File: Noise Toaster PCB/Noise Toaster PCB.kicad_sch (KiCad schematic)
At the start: 0 parts

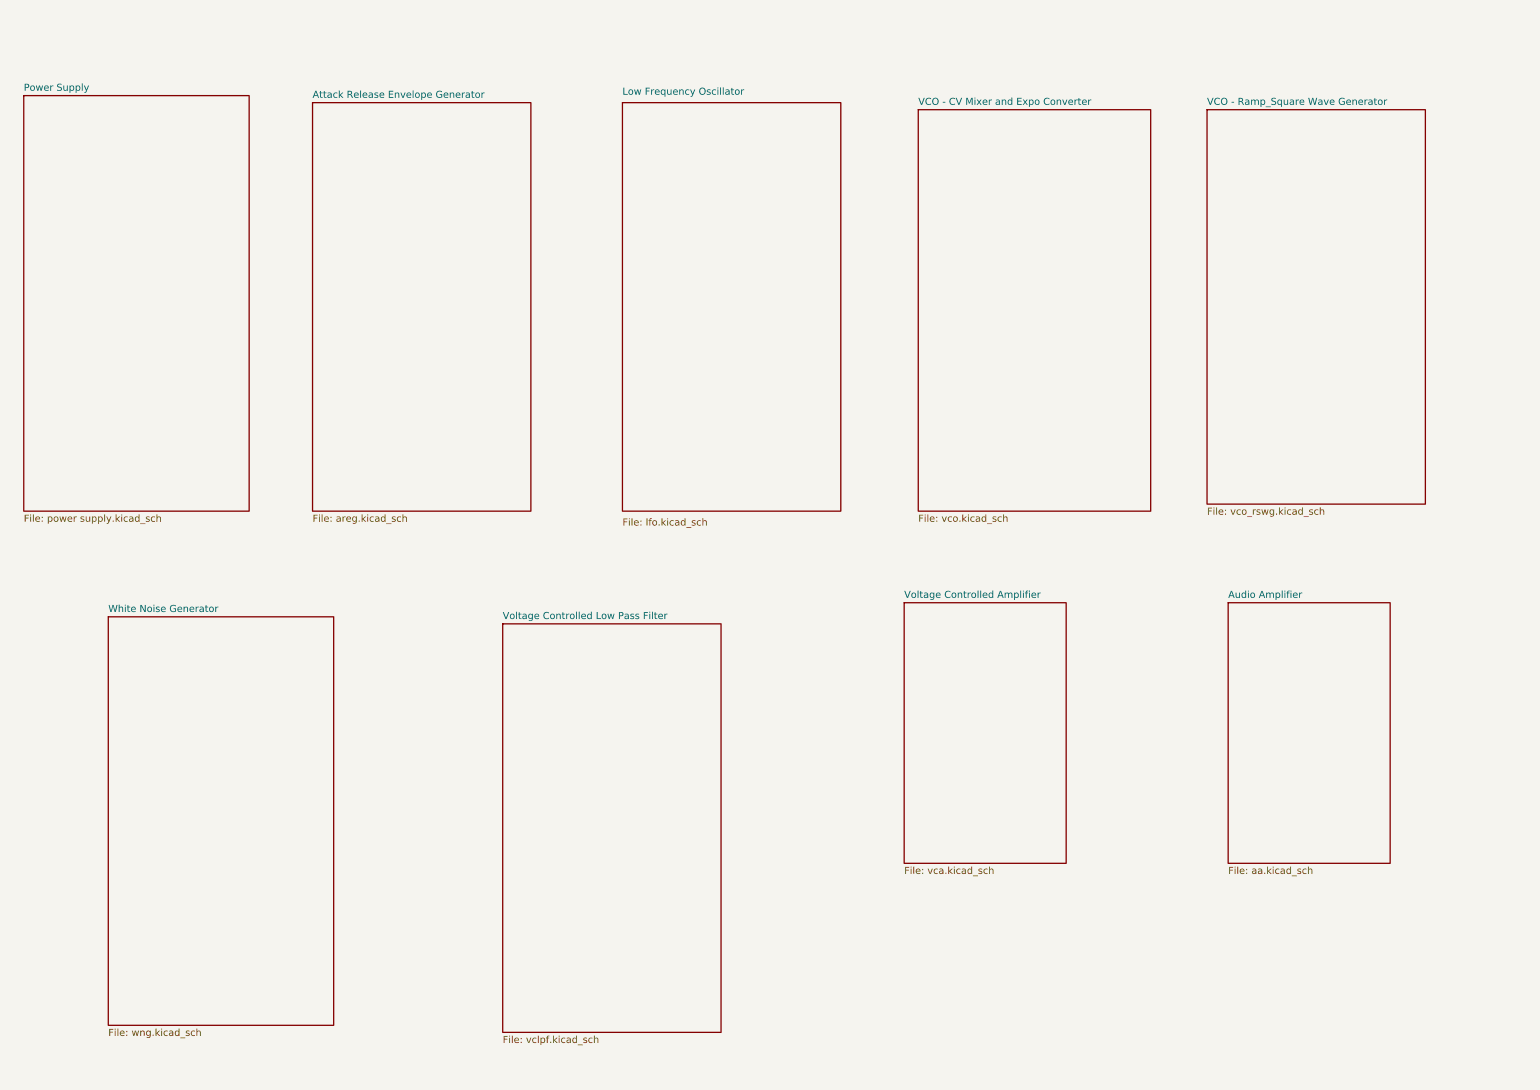
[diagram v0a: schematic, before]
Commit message: updated schematics
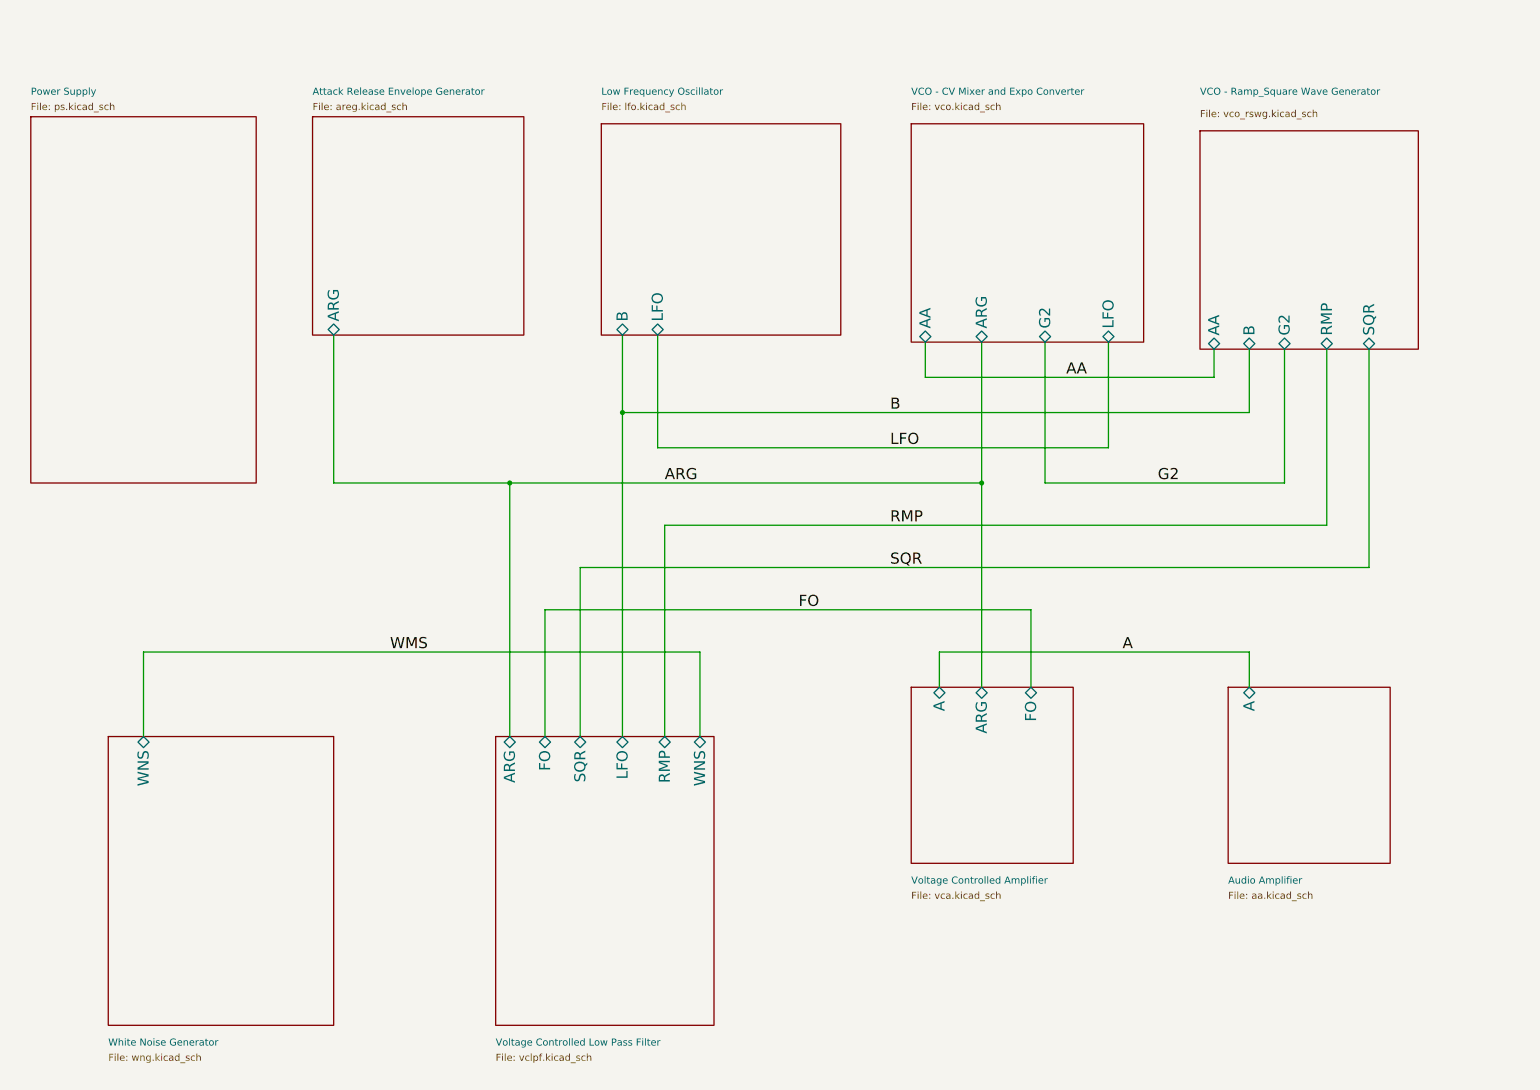
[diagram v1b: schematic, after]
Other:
- sheet Attack Release Envelope Generator ports: added ARG; removed none
- sheet Audio Amplifier ports: added A; removed none
- sheet Low Frequency Oscillator ports: added B, LFO; removed none
- sheet Power Supply: file power supply.kicad_sch -> ps.kicad_sch
- sheet VCO - CV Mixer and Expo Converter ports: added AA, ARG, G2, LFO; removed none
- sheet VCO - Ramp_Square Wave Generator ports: added AA, B, G2, RMP, SQR; removed none
- sheet Voltage Controlled Amplifier ports: added A, ARG, FO; removed none
- sheet Voltage Controlled Low Pass Filter ports: added ARG, FO, LFO, RMP, SQR, WNS; removed none
- sheet White Noise Generator ports: added WNS; removed none

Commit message: refactored the schematic
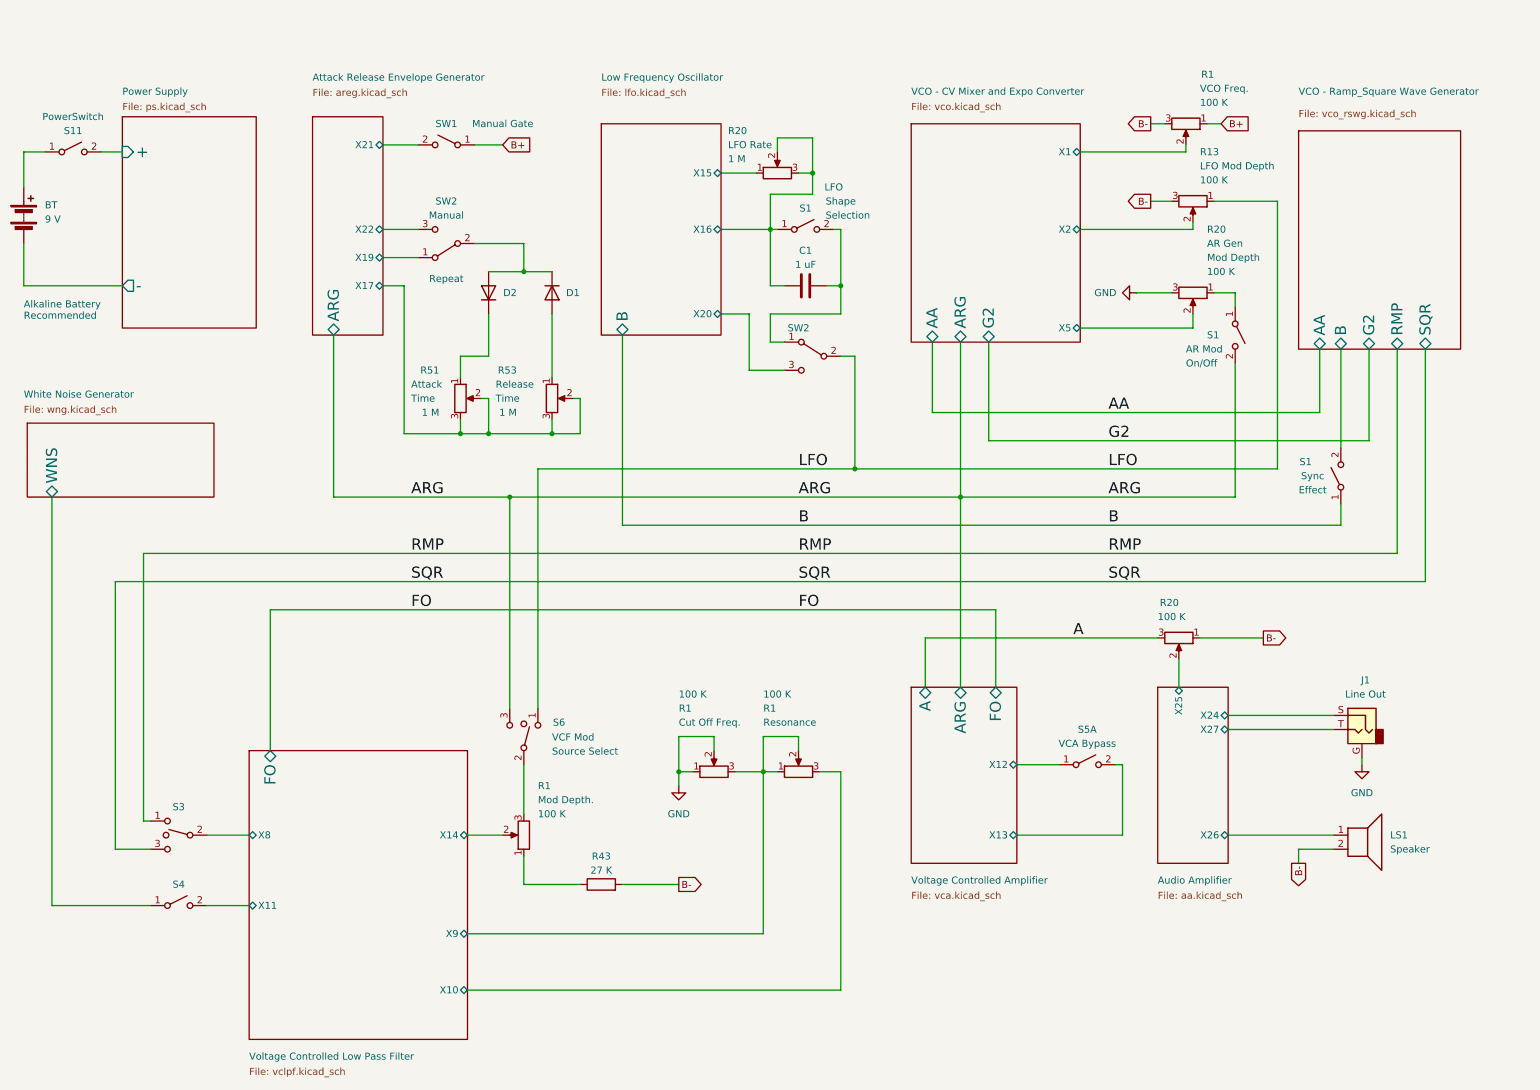
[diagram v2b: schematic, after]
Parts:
- added BT: 9 V, symbol Device:Battery
- added C1: 1 uF, symbol Device:C
- added D1, D2: D, symbol Device:D
- added J1: Line Out, symbol Connector_Audio:AudioJack2_Ground
- added LS1: Speaker, symbol Device:Speaker
- added PowerSwitch: S11, symbol Switch:SW_SPST
- added R1 (x4), R13, R20 (x2): 100 K, symbol Device:R_Potentiometer
- added R20, R51, R53: 1 M, symbol Device:R_Potentiometer
- added R43: 27 K, symbol Device:R
- added S1: LFO, symbol Switch:SW_SPST
- added S1: Sync, symbol Switch:SW_SPST
- added S1: AR Mod, symbol Switch:SW_SPST
- added S3: ~, symbol Switch:SW_SPDT_MSM
- added S4: SW_SPST, symbol Switch:SW_SPST
- added S5: VCA Bypass, symbol Switch:SW_DPST_x2
- added S6: VCF Mod, symbol Switch:SW_SPDT_MSM
- added SW1: Manual Gate, symbol Switch:SW_SPST
- added SW2: ~, symbol Switch:SW_SPDT
- added SW2: Repeat, symbol Switch:SW_SPDT
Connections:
- net A: now also R20.3
- net ARG: now also S1.2 (B), S6.3
- net B: now also S1.1 (A)
- net LFO: now also R13.1, S6.1, SW2.2 (B)
- net RMP: now also S3.1
- net SQR: now also S3.3
- new net: C1.2, S1.2 (B), SW2.1 (A)
- new net: D1.2 (A), R53.1
- new net: D2.1 (K), R51.1
- new net: D1.1 (K), D2.2 (A), SW2.2 (B)
- new net: R1.3, S6.2
- new net: R20.1, S1.1 (A)
- new net: BT.1 (+), PowerSwitch.1 (A)
- new net: R1.1, R43.1
- new net Attack Release Envelope Generator/X17: R51.2, R51.3, R53.2, R53.3
- new net Attack Release Envelope Generator/X19: SW2.1 (A)
- new net Attack Release Envelope Generator/X21: SW1.2 (B)
- new net Attack Release Envelope Generator/X22: SW2.3 (C)
- new net Audio Amplifier/X24: J1.S
- new net Audio Amplifier/X25: R20.2
- new net Audio Amplifier/X26: LS1.1
- new net Audio Amplifier/X27: J1.T
- new net B+: R1.1, SW1.1 (A)
- new net B-: LS1.2, R1.3, R13.3, R20.1, R43.2
- new net GND: J1.G, R1.1, R1.2, R20.3
- new net Low Frequency Oscillator/X15: R20.1
- new net Low Frequency Oscillator/X16: C1.1, R20.2, R20.3, S1.1 (A)
- new net Low Frequency Oscillator/X20: SW2.3 (C)
- new net Power Supply/+: PowerSwitch.2 (B)
- new net Power Supply/-: BT.2 (-)
- new net VCO - CV Mixer and Expo Converter/X1: R1.2
- new net VCO - CV Mixer and Expo Converter/X2: R13.2
- new net VCO - CV Mixer and Expo Converter/X5: R20.2
- new net VCO - Ramp_Square Wave Generator/B: S1.2 (B)
- new net Voltage Controlled Amplifier/X12: S5.1 (A)
- new net Voltage Controlled Amplifier/X13: S5.2 (B)
- new net Voltage Controlled Low Pass Filter/X10: R1.3
- new net Voltage Controlled Low Pass Filter/X11: S4.2 (B)
- new net Voltage Controlled Low Pass Filter/X14: R1.2
- new net Voltage Controlled Low Pass Filter/X8: S3.2
- new net Voltage Controlled Low Pass Filter/X9: R1.1, R1.2, R1.3
- new net White Noise Generator/WNS: S4.1 (A)
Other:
- sheet Attack Release Envelope Generator ports: added X17, X19, X21, X22; removed none
- sheet Audio Amplifier ports: added X24, X25, X26, X27; removed A
- sheet Low Frequency Oscillator ports: added X15, X16, X20; removed LFO
- sheet Power Supply ports: added +, -; removed none
- sheet VCO - CV Mixer and Expo Converter ports: added X1, X2, X5; removed LFO
- sheet Voltage Controlled Amplifier ports: added X12, X13; removed none
- sheet Voltage Controlled Low Pass Filter ports: added X10, X11, X14, X8, X9; removed ARG, LFO, RMP, SQR, WNS
- note added: "Alkaline Battery Recommended"

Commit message: refactored schematics and added front panel
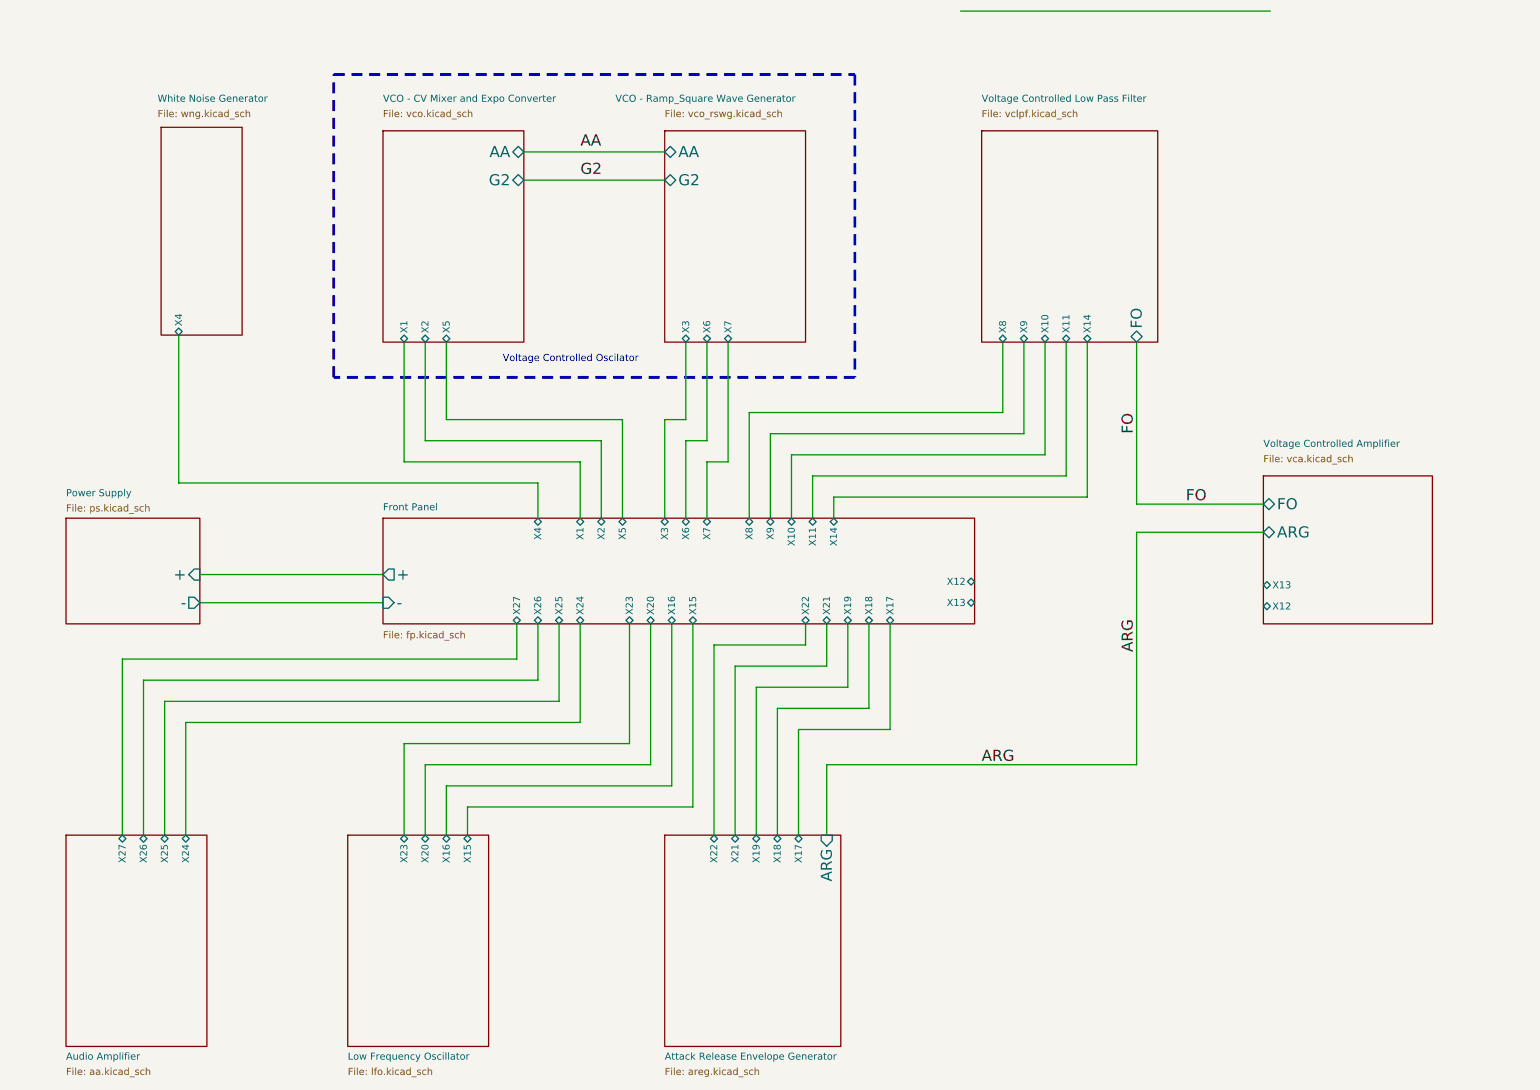
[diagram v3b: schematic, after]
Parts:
- removed BT: 9 V, symbol Device:Battery
- removed C1: 1 uF, symbol Device:C
- removed D1, D2: D, symbol Device:D
- removed J1: Line Out, symbol Connector_Audio:AudioJack2_Ground
- removed LS1: Speaker, symbol Device:Speaker
- removed PowerSwitch: S11, symbol Switch:SW_SPST
- removed R1 (x4), R13, R20 (x2): 100 K, symbol Device:R_Potentiometer
- removed R20, R51, R53: 1 M, symbol Device:R_Potentiometer
- removed R43: 27 K, symbol Device:R
- removed S1: LFO, symbol Switch:SW_SPST
- removed S1: Sync, symbol Switch:SW_SPST
- removed S1: AR Mod, symbol Switch:SW_SPST
- removed S3: ~, symbol Switch:SW_SPDT_MSM
- removed S4: SW_SPST, symbol Switch:SW_SPST
- removed S5: VCA Bypass, symbol Switch:SW_DPST_x2
- removed S6: VCF Mod, symbol Switch:SW_SPDT_MSM
- removed SW1: Manual Gate, symbol Switch:SW_SPST
- removed SW2: ~, symbol Switch:SW_SPDT
- removed SW2: Repeat, symbol Switch:SW_SPDT
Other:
- added sheet Front Panel (fp.kicad_sch)
- sheet Attack Release Envelope Generator ports: added X18; removed none
- sheet Low Frequency Oscillator ports: added X23; removed B
- sheet VCO - CV Mixer and Expo Converter ports: added none; removed ARG
- sheet VCO - Ramp_Square Wave Generator ports: added X3, X6, X7; removed B, RMP, SQR
- sheet Voltage Controlled Amplifier ports: added none; removed A
- sheet White Noise Generator ports: added X4; removed WNS
- note added: "Voltage Controlled Oscilator"
- note removed: "Alkaline Battery Recommended"
